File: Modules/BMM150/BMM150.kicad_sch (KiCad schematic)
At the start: 4 parts, among them U1 BMM150

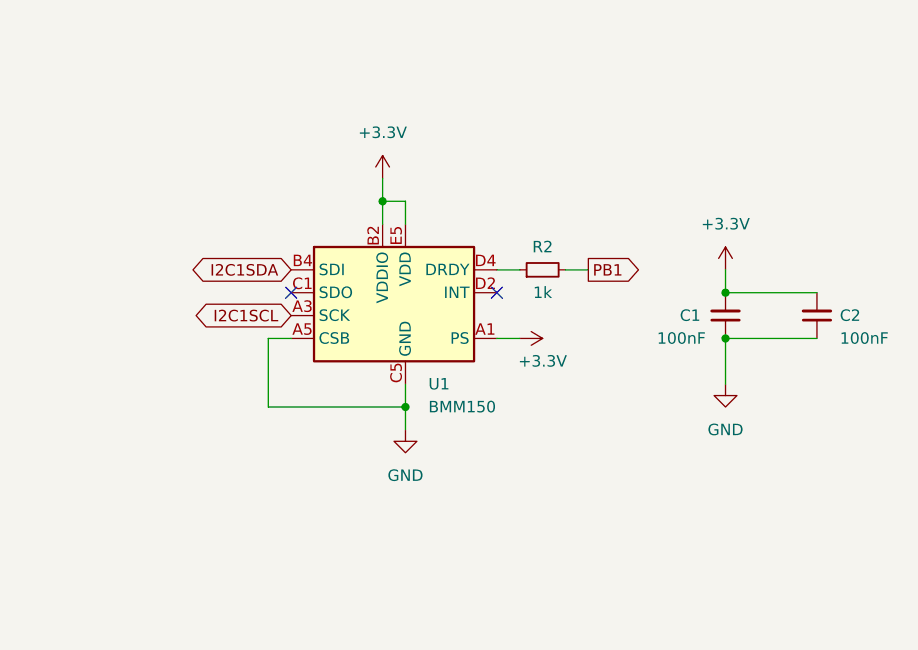
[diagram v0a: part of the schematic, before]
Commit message: BMM150 updated.
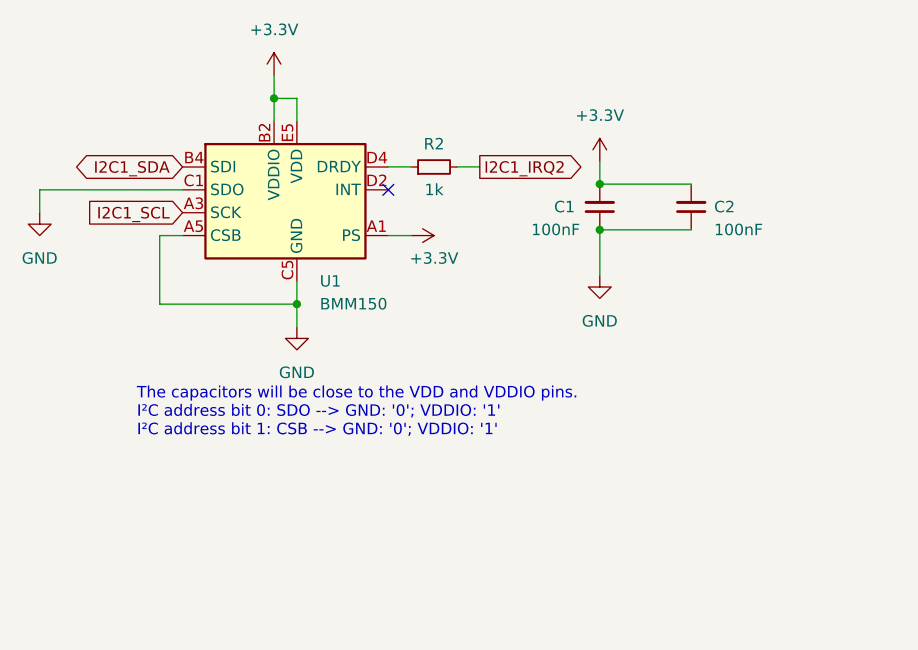
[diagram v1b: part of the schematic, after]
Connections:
- net GND: now also U1.C1 (SDO)
- net I2C1SCL renamed I2C1_SCL 
- net I2C1SDA renamed I2C1_SDA 
- net PB1 renamed I2C1_IRQ2
- no-connect marks 2 -> 1
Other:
- note added: "The capacitors will be close to the VDD and VDDIO pins. I²C address bit 0: SDO --> GND: '0'; VDDIO: '1' I²C address bit 1: CSB --> GND: '0'; VDDIO: '1'"
- moved on the sheet: C1, C2, R2, U1
